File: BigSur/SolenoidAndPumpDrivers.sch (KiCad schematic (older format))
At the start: 54 parts, among them Q1 TSM900N10, Q2 TSM900N10, U1 DRV103H, U2 DRV103H, U3 DRV8806

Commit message: Chose LEDs.
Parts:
- removed C10, C11, C12, C13, C14: 10uF, Capacitor_SMD:C_1210_3225Metric_Pad1.42x2.65mm_HandSolder, symbol Device:C
- removed D10, D12, D3, D5, D8, D9: LED, symbol Device:LED
- removed R11, R13, R27: R_US, symbol Device:R_US
- removed R16, R17, R18: R_US, Resistor_SMD:R_1210_3225Metric_Pad1.42x2.65mm_HandSolder, symbol Device:R_US
- added C? (x3): 22uF, Capacitor_SMD:C_0603_1608Metric_Pad1.05x0.95mm_HandSolder, symbol Device:C
- added D? (x6): QTLP651C4TR, LED_SMD:LED_1206_3216Metric_Pad1.42x1.75mm_HandSolder, symbol Device:LED
- added R? (x6): 68, Resistor_SMD:R_0603_1608Metric_Pad1.05x0.95mm_HandSolder, symbol Device:R_US
- D11, D7: value LED -> QTLP651C4TR; footprint (none) -> LED_SMD:LED_1206_3216Metric_Pad1.42x1.75mm_HandSolder; Digikey (none) -> https://www.digikey.ca/product-detail/en/everlight-electron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
- R15: value R_US -> 68; footprint Resistor_SMD:R_1210_3225Metric_Pad1.42x2.65mm_HandSolder -> Resistor_SMD:R_0603_1608Metric_Pad1.05x0.95mm_HandSolder; Digikey (none) -> https://www.digikey.ca/product-detail/en/rohm-semiconductor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
- R26: value R_US -> 68; footprint (none) -> Resistor_SMD:R_0603_1608Metric_Pad1.05x0.95mm_HandSolder; Digikey (none) -> https://www.digikey.ca/product-detail/en/rohm-semiconductor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
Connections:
- net +24V: now also C?.1, C?.1, C?.1
- net +3V3: now also R?.1, R?.1, R?.1, R?.1, R?.2, R?.2
- net GND: now also C?.2, C?.2, C?.2
- net PUMP_LS_CHANNEL_2: now also D?.1 (K)
- net SOLENOID_ECONOMIZED_CHANNEL_1_SENSE: now also D?.1 (K)
- net SOLENOID_ECONOMIZED_CHANNEL_2_SENSE: now also D?.1 (K)
- net SOLENOID_LS_CHANNEL_1_SENSE: now also D?.1 (K)
- net SOLENOID_LS_CHANNEL_2_SENSE: now also D?.1 (K)
- net SOLENOID_LS_CHANNEL_3_SENSE: now also D?.1 (K)
- new net: D?.2 (A), R?.1 (x2)
- new net: D?.2 (A), R?.2 (x4)
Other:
- note added: "SHOULD GO TO 5V TOLERANT I/O"
- moved on the sheet: C15, C3, C4, C5, C6, C7, C8, C9, D11, D2, D7, JP2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

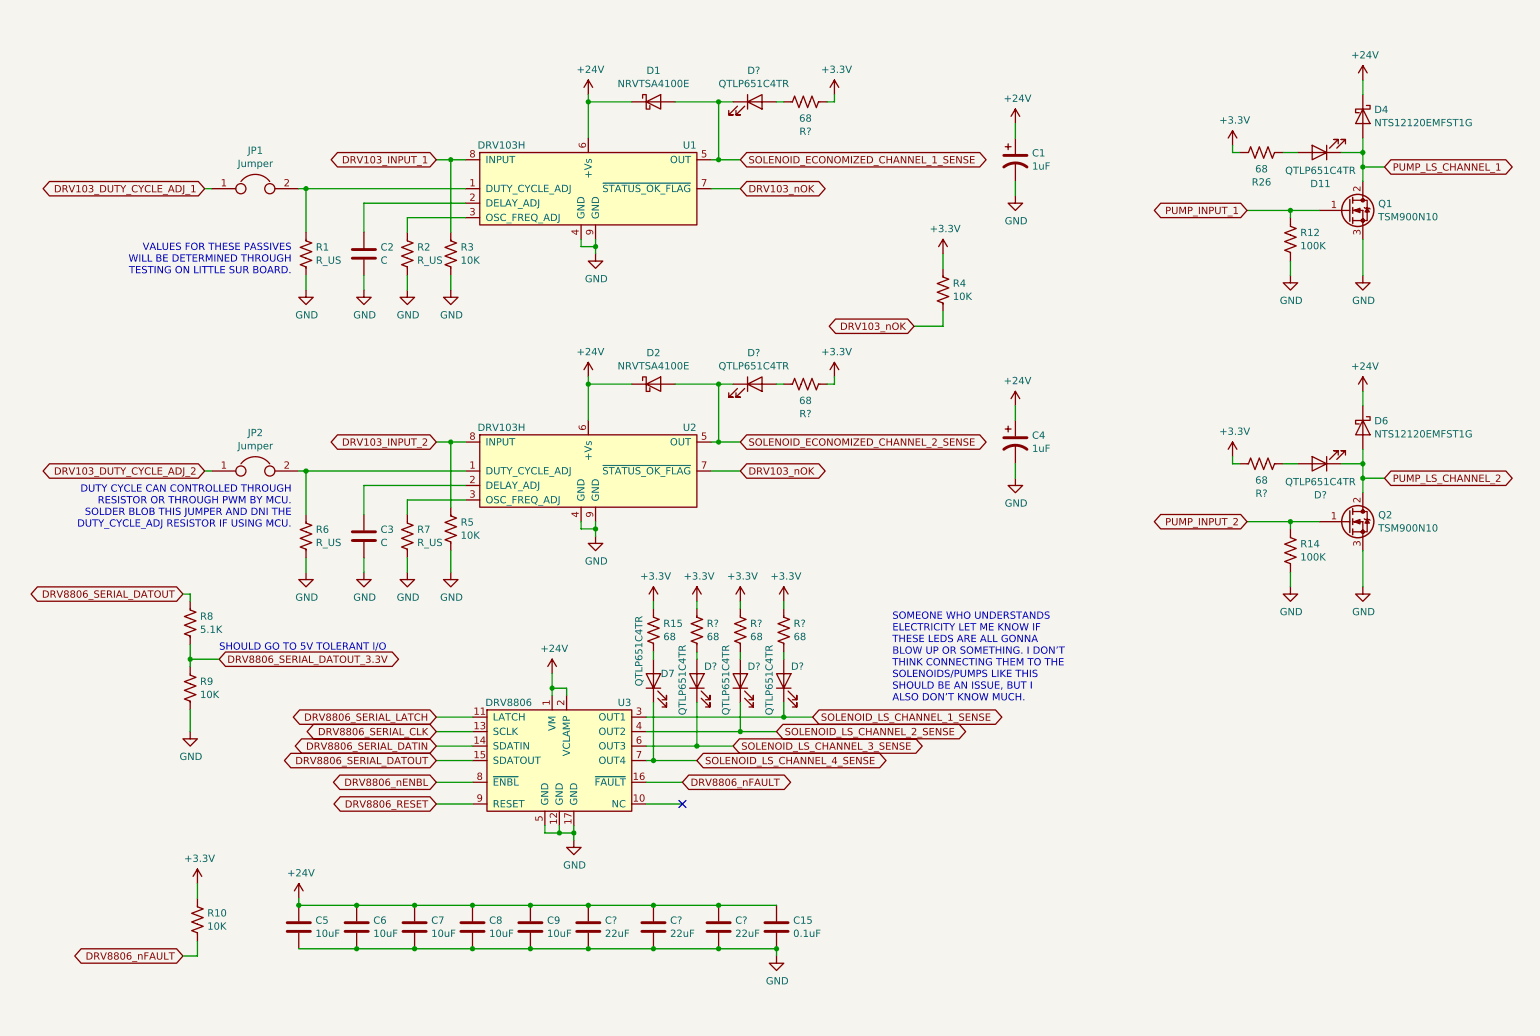
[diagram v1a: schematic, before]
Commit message: Updated test points
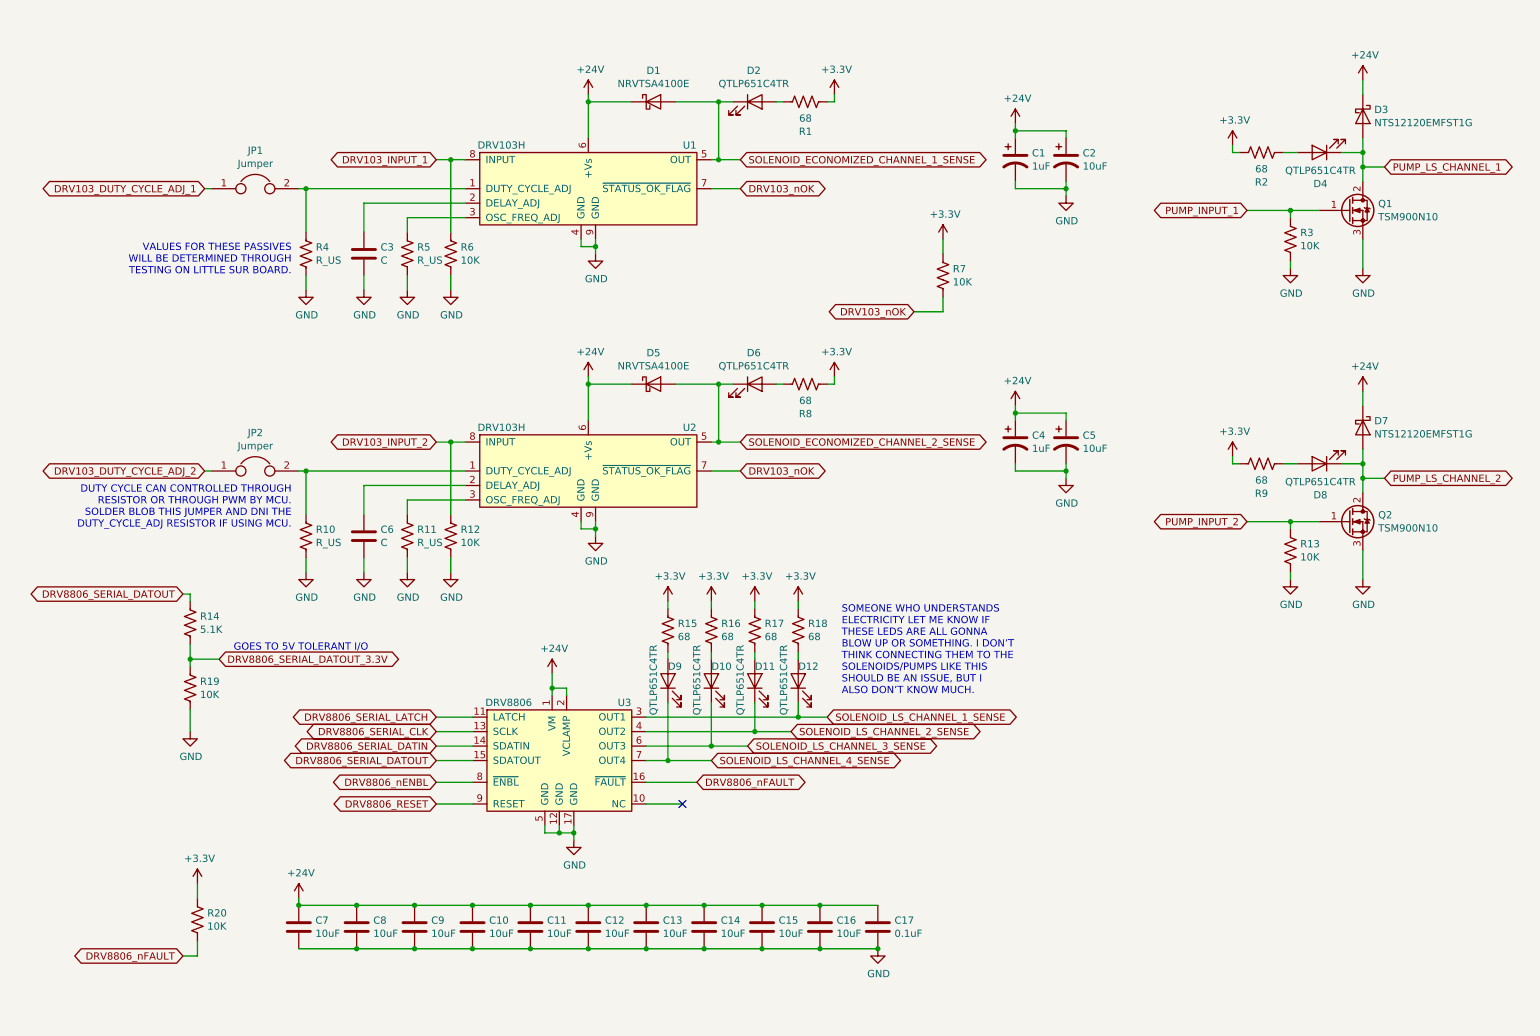
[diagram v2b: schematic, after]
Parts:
- removed C? (x3): 22uF, Capacitor_SMD:C_0603_1608Metric_Pad1.05x0.95mm_HandSolder, symbol Device:C
- removed R10, R4, R9: 10K, Resistor_SMD:R_0603_1608Metric_Pad1.05x0.95mm_HandSolder, symbol Device:R_US
- removed R12, R14: 100K, Resistor_SMD:R_0603_1608Metric_Pad1.05x0.95mm_HandSolder, symbol Device:R_US
- added C12, C13, C14, C15, C16: 10uF, Capacitor_SMD:C_1210_3225Metric_Pad1.42x2.65mm_HandSolder, symbol Device:C
- added C2, C5: 10uF, BigSur:VISHAY_CAP_SMD_293D106X9050E2TE3, symbol Device:CP1
- added R13, R19, R20, R6, R7: 10K, Resistor_SMD:R_0603_1608Metric_Pad1.05x0.95mm_HandSolder, symbol Device:R_US
- R12: renamed from R5; Digikey (none) -> https://www.digikey.ca/product-detail/en/stackpole-electron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; Part Number (none) -> RNCP0603FTD10K0
- R14: renamed from R8; Digikey (none) -> https://www.digikey.ca/product-detail/en/bourns-inc/CR0603-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; Part Number (none) -> CR0603-FX-5101ELF
- R3: Digikey (none) -> https://www.digikey.ca/product-detail/en/stackpole-electron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; Part Number (none) -> RNCP0603FTD10K0
- gave numbers to parts that had none: 12
- renumbered C8 to C10, C9 to C11, C15 to C17, C2 to C3, C3 to C6, C5 to C7, C6 to C8, C7 to C9, D4 to D3, D11 to D4, D2 to D5, D6 to D7, D7 to D9, R6 to R10, R7 to R11, R26 to R2, R1 to R4, R2 to R5
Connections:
- net +24V: now also C12.1, C13.1, C14.1, C15.1, C16.1, C2.1, C5.1
- net +3V3: now also R20.1, R7.1
- net DRV103_INPUT_1: now also R6.1; no longer R3.1
- net DRV103_nOK: now also R7.2
- net DRV8806_SERIAL_DATOUT_3.3V: now also R19.1
- net DRV8806_nFAULT: now also R20.2
- net GND: now also C12.2, C13.2, C14.2, C15.2, C16.2, C2.2, C5.2, R13.2, R19.2, R6.2
- net PUMP_INPUT_1: now also R3.1
- net PUMP_INPUT_2: now also R13.1
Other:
- note added: "GOES TO 5V TOLERANT I/O"
- note removed: "SHOULD GO TO 5V TOLERANT I/O"
- moved on the sheet: C17, D10, D11, D12, D9, R12, R15, R16, R17, R18

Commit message: Added braking detection, relay flyback, changed current sensors.
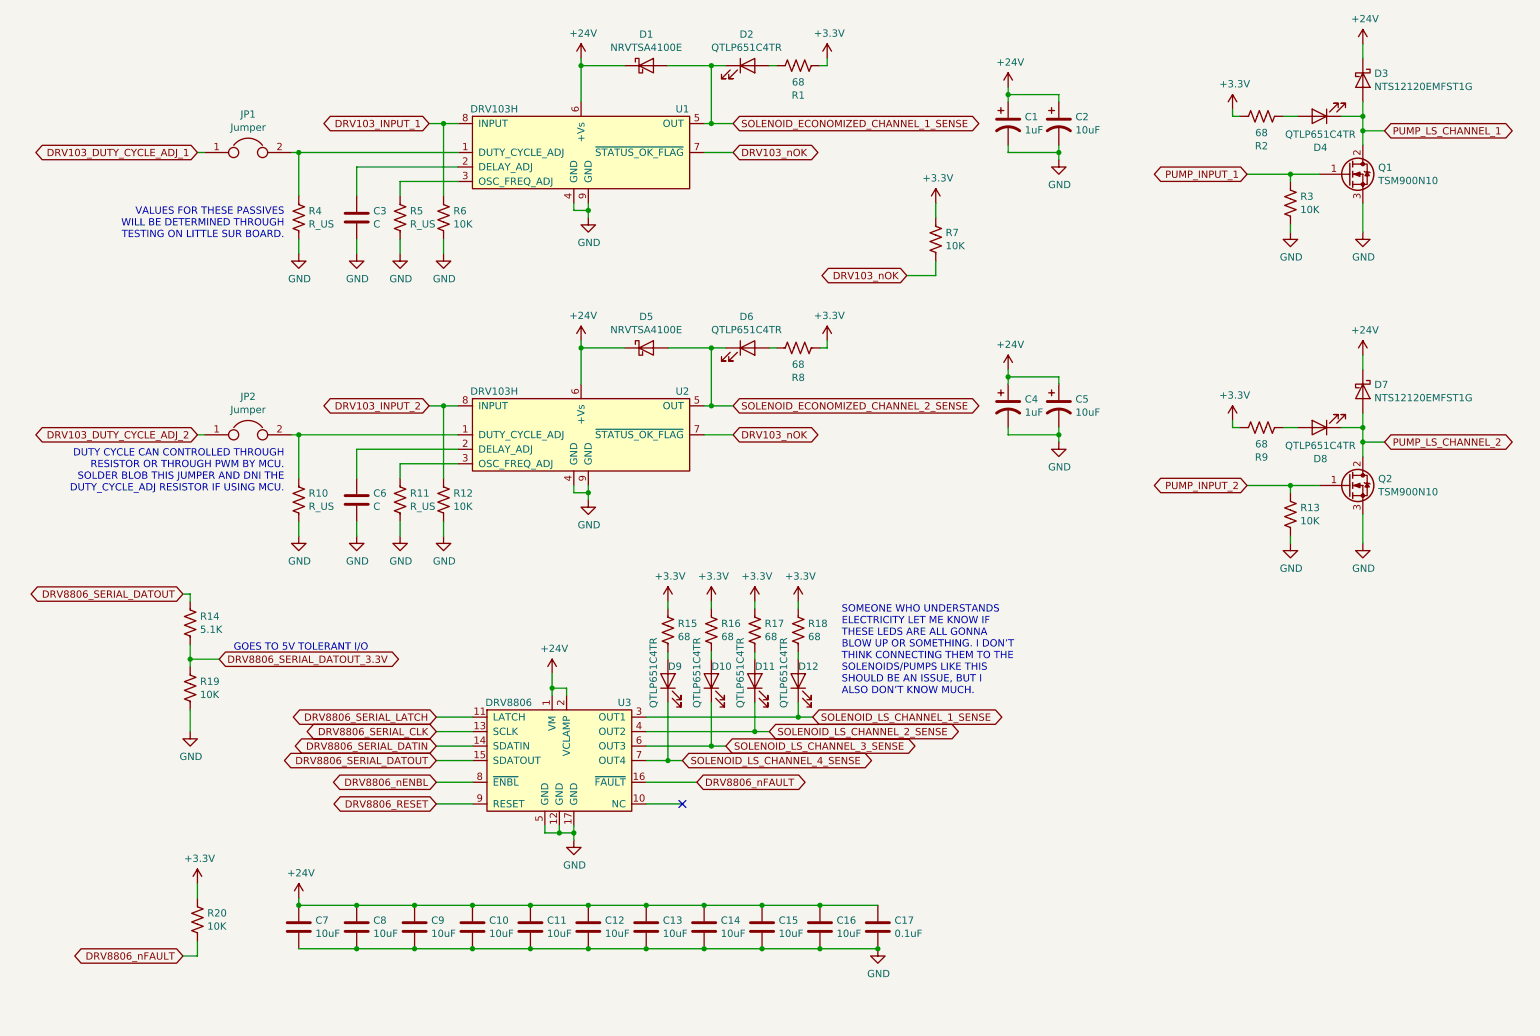
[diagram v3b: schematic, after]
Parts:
- R1, R15, R16, R17, R18, R2, R8, R9: Part Number (none) -> ESR03EZPJ680
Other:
- moved on the sheet: C1, C2, C3, C4, C5, C6, D1, D2, D3, D4, D5, D6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

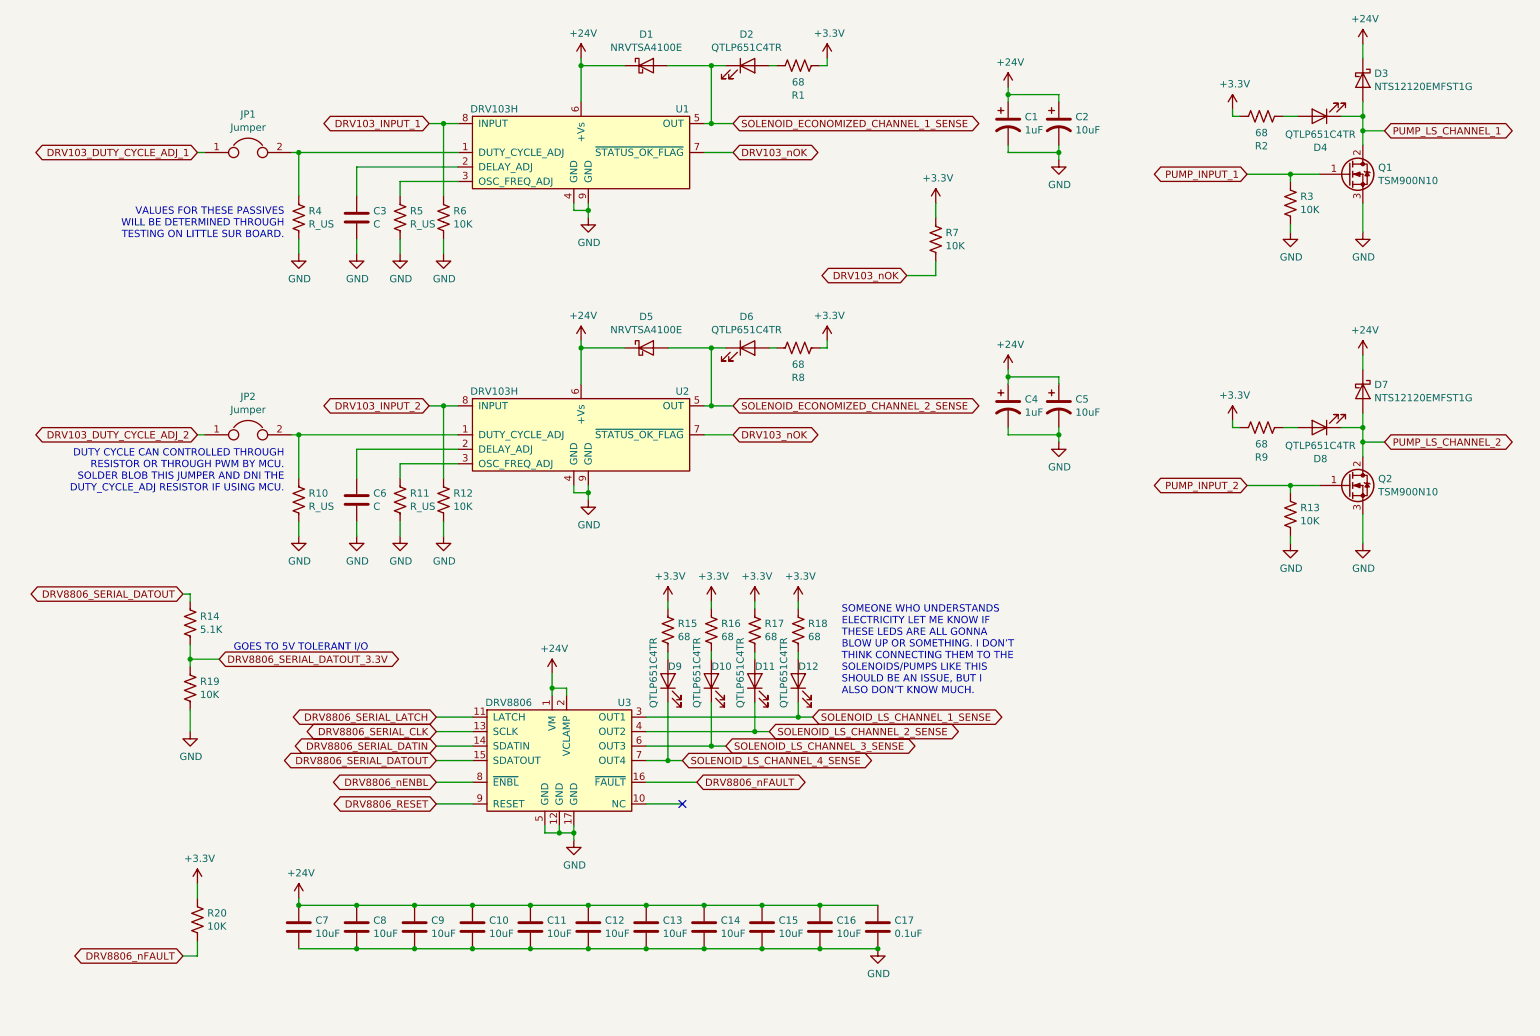
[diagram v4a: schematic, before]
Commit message: Switched to active low brake lines
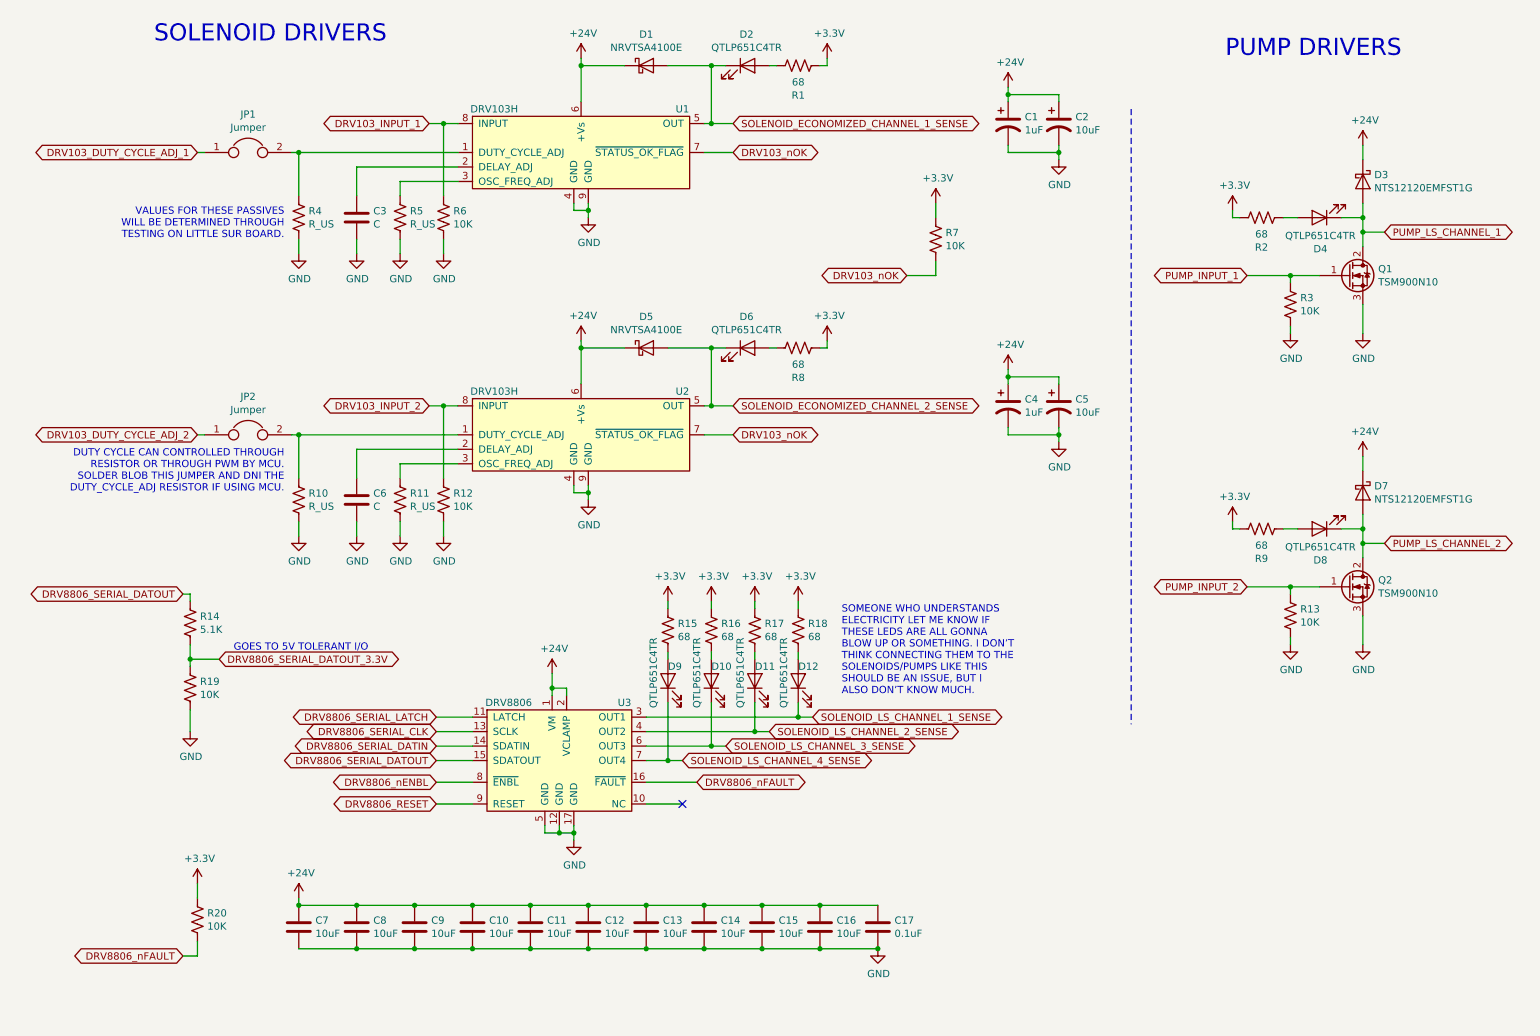
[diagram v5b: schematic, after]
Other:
- note added: "PUMP DRIVERS"
- note added: "SOLENOID DRIVERS"
- moved on the sheet: D3, D4, D7, D8, Q1, Q2, R13, R2, R3, R9
